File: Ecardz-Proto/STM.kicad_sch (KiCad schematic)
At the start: 35 parts, among them J1 Conn_02x06_Odd_Even, J3 Conn_ARM_SWD_TagConnect_TC203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, J4 Conn_02x07_Odd_Even, U1 STM32L071K8Ux

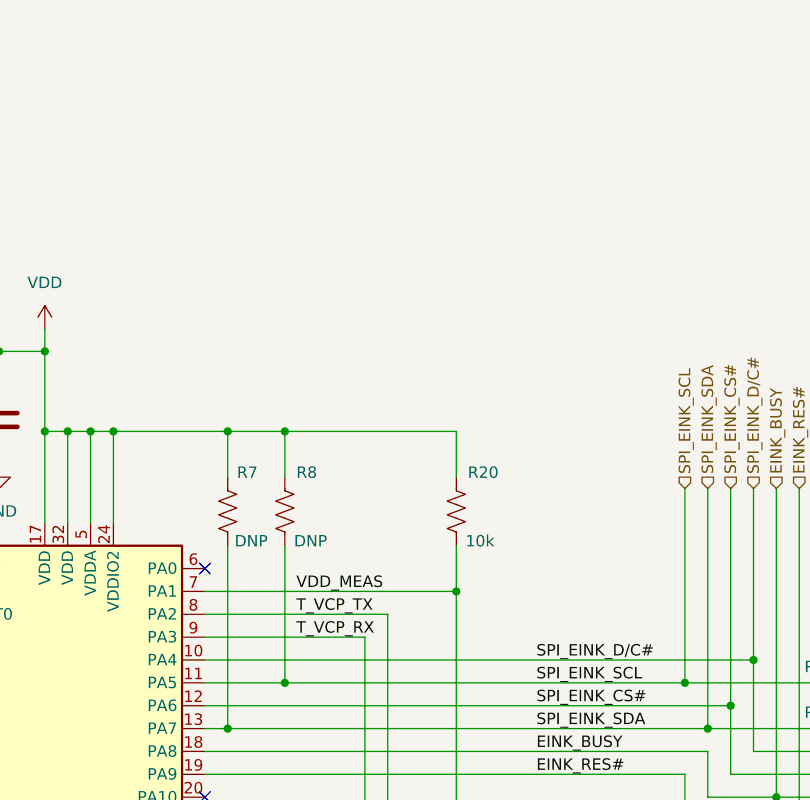
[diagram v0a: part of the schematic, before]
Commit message: added zener and extra cap footprints
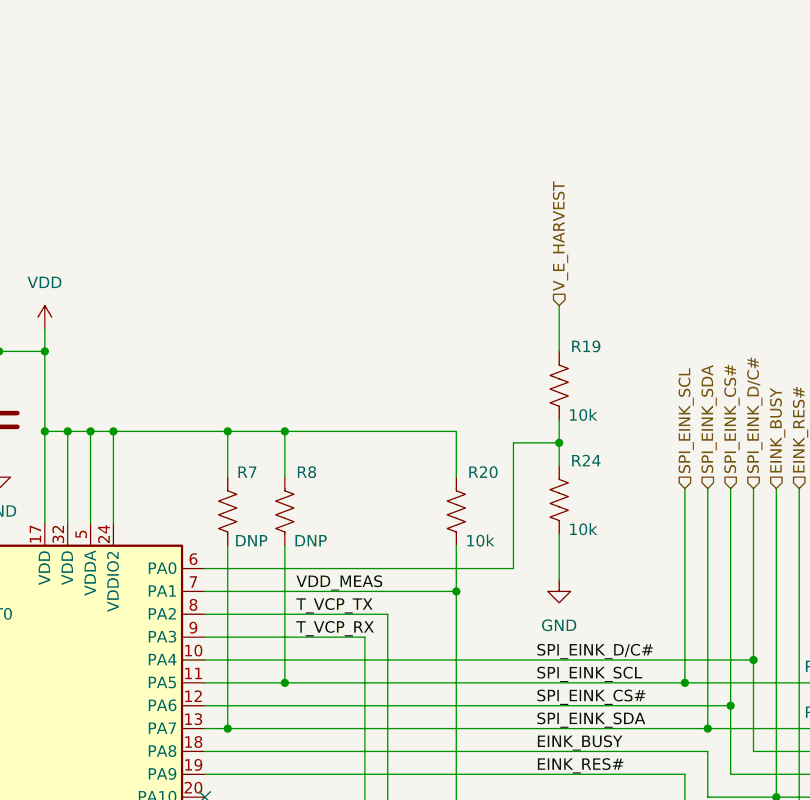
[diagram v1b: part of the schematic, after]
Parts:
- added R19, R24: 10k, Resistor_SMD:R_0603_1608Metric_Pad0.98x0.95mm_HandSolder, symbol Device:R_US
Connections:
- net GND: now also R24.2
- net at U1.6 (PA0): now also R19.2, R24.1
- new net V_E_HARVEST: R19.1
- no-connect marks 13 -> 12

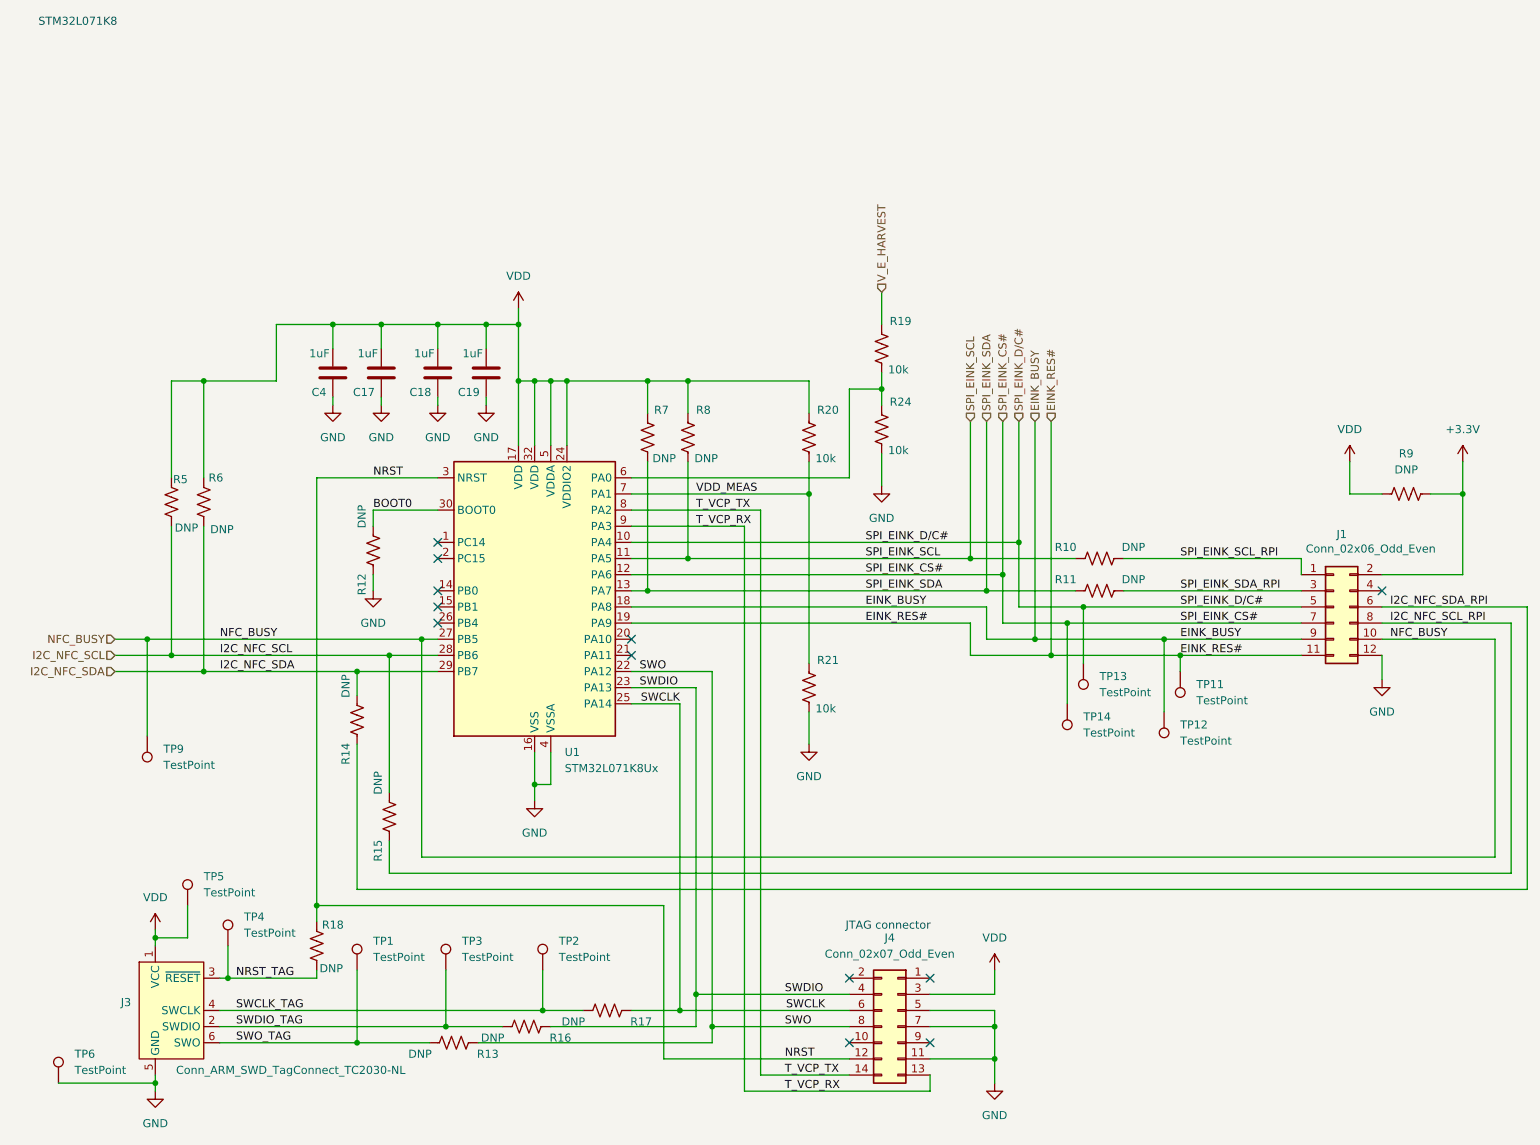
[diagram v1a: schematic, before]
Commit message: added parts numbers for everything
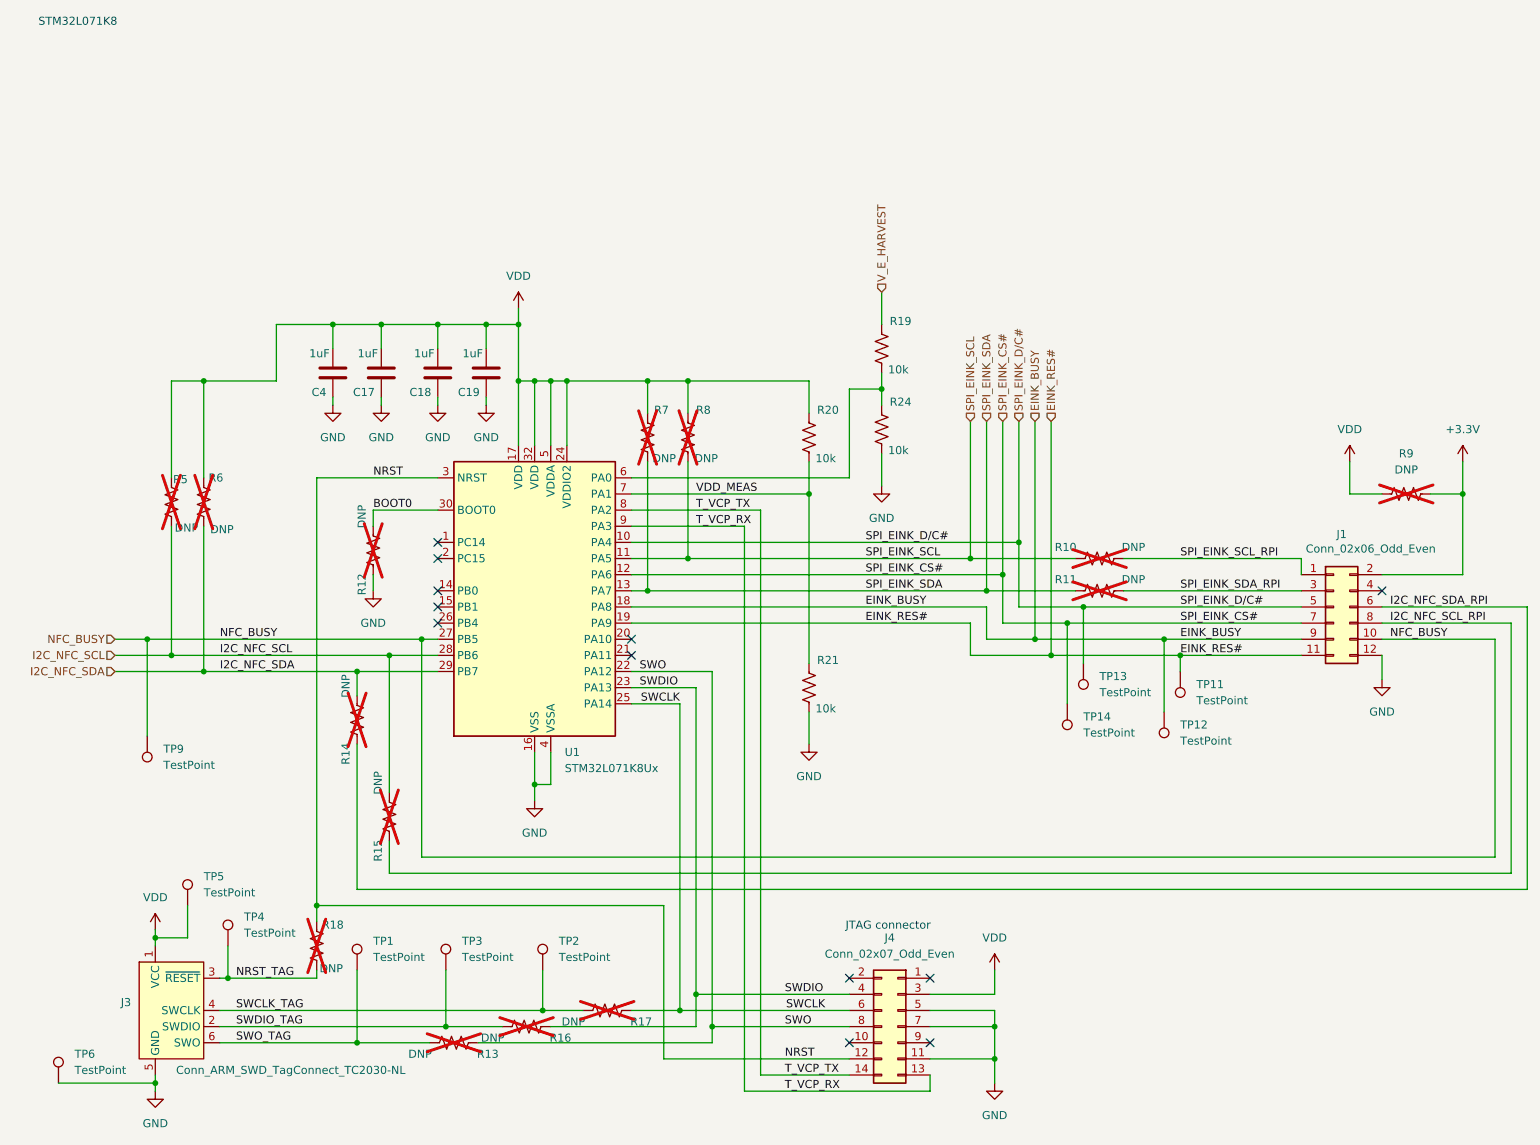
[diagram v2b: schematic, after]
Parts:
- C17, C18, C19, C4: Digikey Part Number (none) -> 311-1445-2-ND
- J1: Digikey Part Number (none) -> 2057-PH2-12-UA-ND; MANUFACTURER PART NUMBER (none) -> PH2-12-UA; Mouser Part Number (none) -> 732-5297-ND
- J4: Digikey Part Number (none) -> 1175-1632-ND; MANUFACTURER PART NUMBER (none) -> 3220-14-0300-00
- R10, R11, R12, R13, R14, R15, R16, R17, R18, R5, R6, R7, R8, R9: now not fitted
- R19, R20, R21, R24: Digikey Part Number (none) -> 311-10.0KHRTR-ND; MANUFACTURER PART NUMBER 100kR -> RC0603FR-0710KL
- U1: Digikey Part Number (none) -> 497-18576-ND; MANUFACTURER PART NUMBER (none) -> STM32L071K8U6
